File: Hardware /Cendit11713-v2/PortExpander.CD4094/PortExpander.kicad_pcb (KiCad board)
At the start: 2 copper layers, 14 parts, among them P1 CONN_01X06, P2 CONN_01X07, P3 CONN_01X07, U1 CD4094BE, U2 ULN2003A, U3 CD4094BE, U4 ULN2003A

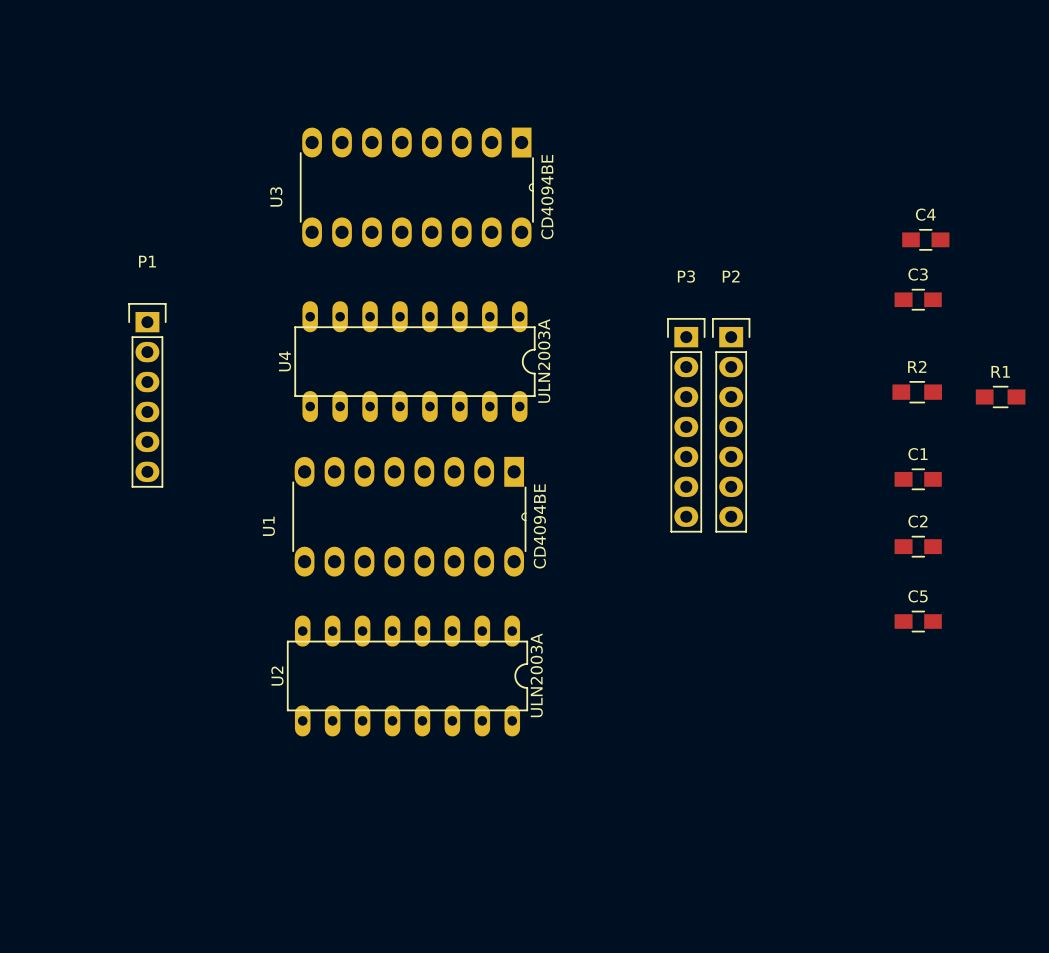
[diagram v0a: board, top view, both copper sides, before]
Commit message: En Cendit11713 + CenditLab respaldo
  - Se revisan tarjetas
  - Correccion en PCB GPIB
  - Se inicia tarjeta madre en una pieza (MainBoard.OnePiece)
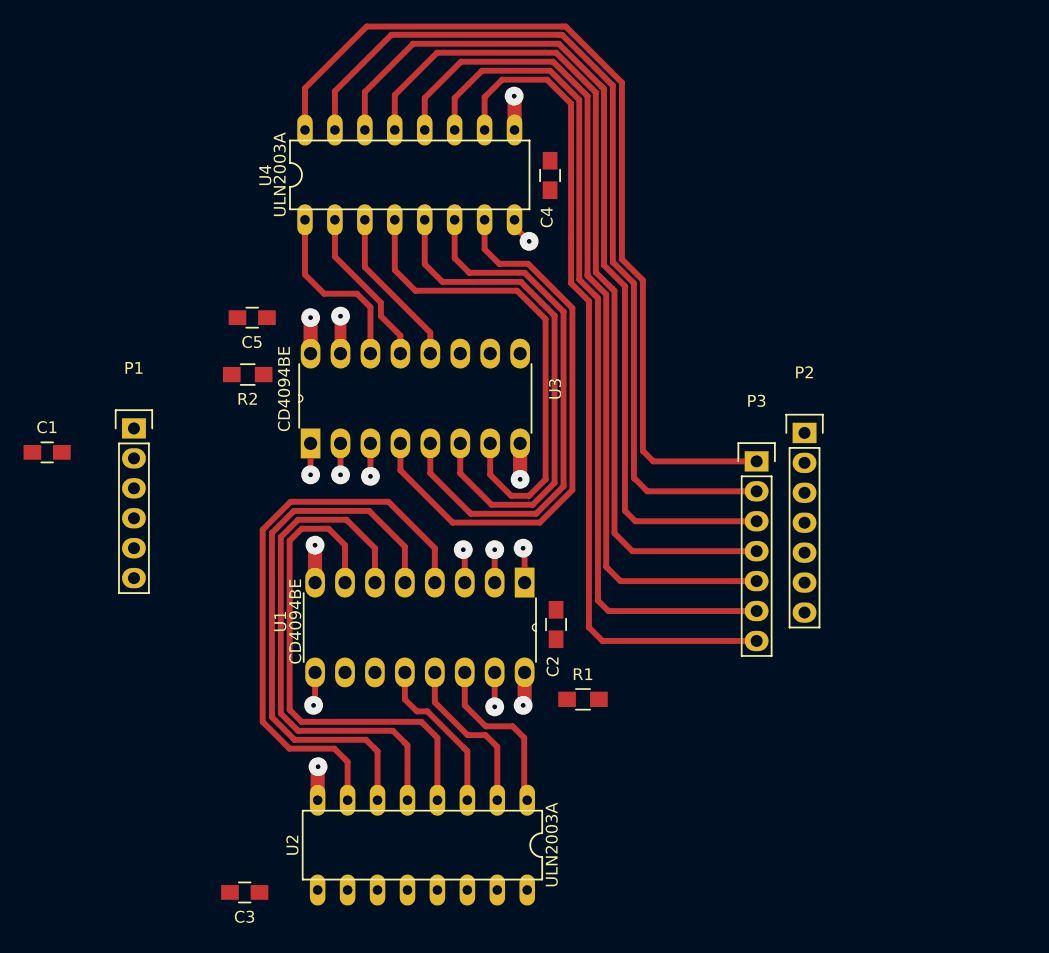
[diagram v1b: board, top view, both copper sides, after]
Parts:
- moved C3 76.1 mm to (91.4, 147.4), turned to 180 degrees
- moved C1 73.9 mm to (74.7, 110.1)
- moved C5 62.1 mm to (92.1, 98.7), turned to 180 degrees
- moved R2 56.8 mm to (91.7, 103.5), turned to 180 degrees
- moved R1 43.7 mm to (120.1, 131.1)
- moved C4 32.3 mm to (117.3, 86.6), turned to 270 degrees
- moved C2 31.4 mm to (117.9, 124.7), turned to 90 degrees
- moved U4 29.3 mm to (115.4, 83.6), turned to 90 degrees
- moved U3 20.4 mm to (114.8, 101.7), turned to 90 degrees
- moved U2 14.4 mm to (96.5, 146.4)
- moved P3 12.1 mm to (134.9, 110.9)
- moved P2 10.2 mm to (138.9, 108.5)
- moved U1 9.44 mm to (97.4, 128.8)
- moved P1 9.09 mm to (82.0, 108.1)
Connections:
- net Net-(U1-Pad7) renamed /Q3
- net Net-(U1-Pad9) renamed /CAS_HI
- net Net-(U3-Pad7) renamed /Q9
- P1 pad 1: (no net) -> VDD
- P1 pad 2: (no net) -> GNDPWR
- P1 pad 3: (no net) -> /DATA_IN
- P1 pad 4: (no net) -> /CLK
- P1 pad 5: (no net) -> /STRB
- P1 pad 6: (no net) -> /OE
- P2 pad 1: /P0 -> /P6
- P2 pad 2: /P1 -> /P5
- P2 pad 3: /P2 -> /P4
- P2 pad 5: /P4 -> /P2
- P2 pad 6: /P5 -> /P1
- P2 pad 7: /P6 -> /P0
- U1 pad 10: (no net) -> Net-(U1-Pad10)
- U1 pad 11: (no net) -> Net-(U1-Pad11)
- U1 pad 12: Net-(U1-Pad12) -> /Q6
- U1 pad 13: Net-(U1-Pad13) -> /Q5
- U1 pad 14: Net-(U1-Pad14) -> /Q4
- U1 pad 2: (no net) -> /DATA_IN
- U1 pad 4: Net-(U1-Pad4) -> /Q0
- U1 pad 5: Net-(U1-Pad5) -> /Q1
- U1 pad 6: Net-(U1-Pad6) -> /Q2
- U2 pad 1: Net-(U1-Pad4) -> /Q4
- U2 pad 2: Net-(U1-Pad5) -> /Q5
- U2 pad 3: Net-(U1-Pad6) -> /Q6
- U2 pad 5: Net-(U1-Pad14) -> /Q2
- U2 pad 6: Net-(U1-Pad13) -> /Q1
- U2 pad 7: Net-(U1-Pad12) -> /Q0
- U3 pad 10: (no net) -> Net-(U3-Pad10)
- U3 pad 11: (no net) -> Net-(U3-Pad11)
- U3 pad 12: Net-(U3-Pad12) -> /Q12
- U3 pad 13: Net-(U3-Pad13) -> /Q11
- U3 pad 14: Net-(U3-Pad14) -> /Q10
- U3 pad 4: Net-(U3-Pad4) -> /Q6
- U3 pad 5: Net-(U3-Pad5) -> /Q7
- U3 pad 6: Net-(U3-Pad6) -> /Q8
- U3 pad 9: (no net) -> Net-(U3-Pad9)
- U4 pad 1: Net-(U3-Pad4) -> /Q10
- U4 pad 2: Net-(U3-Pad5) -> /Q11
- U4 pad 3: Net-(U3-Pad6) -> /Q12
- U4 pad 5: Net-(U3-Pad14) -> /Q8
- U4 pad 6: Net-(U3-Pad13) -> /Q7
- U4 pad 7: Net-(U3-Pad12) -> /Q6
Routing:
- net /P7: track 0.00 -> 76.6 mm
- net /P8: track 0.00 -> 75.6 mm
- net /P9: track 0.00 -> 74.9 mm
- net /P10: track 0.00 -> 73.7 mm
- net /P11: track 0.00 -> 72.9 mm
- net /P12: track 0.00 -> 72.2 mm
- net /P13: track 0.00 -> 71.3 mm
- net /Q6: track 0.00 -> 60.9 mm
- net /Q0: track 0.00 -> 48.3 mm
- net /Q1: track 0.00 -> 46.3 mm
- net /Q7: track 0.00 -> 45.4 mm
- net /Q2: track 0.00 -> 44.0 mm
- net /Q8: track 0.00 -> 43.2 mm
- net /Q3: track 0.00 -> 42.0 mm
- net /Q9: track 0.00 -> 41.1 mm
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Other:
- net class DSIGNAL added: clearance 0.25, trace_width 0.5, via_dia 1.6, via_drill 0.4
- net class POWER added: clearance 0.3, trace_width 1.2, via_dia 1.6, via_drill 0.4
